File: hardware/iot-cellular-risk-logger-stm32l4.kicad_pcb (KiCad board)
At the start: 4 copper layers, 79 x 66.1 mm, 96 parts, among them J1 Nano SIM, J2 U.FL Antenna Connector (Male), J3 GSM_USB, J4 USB Type-C, J5 TagConnect SWD ARM, J6 GSM_DEBUG_UART, Q1 IRLML6401, Q2 DTC143Z, U1 STM32L433CBUx, U10 BGA 524N6 E6327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

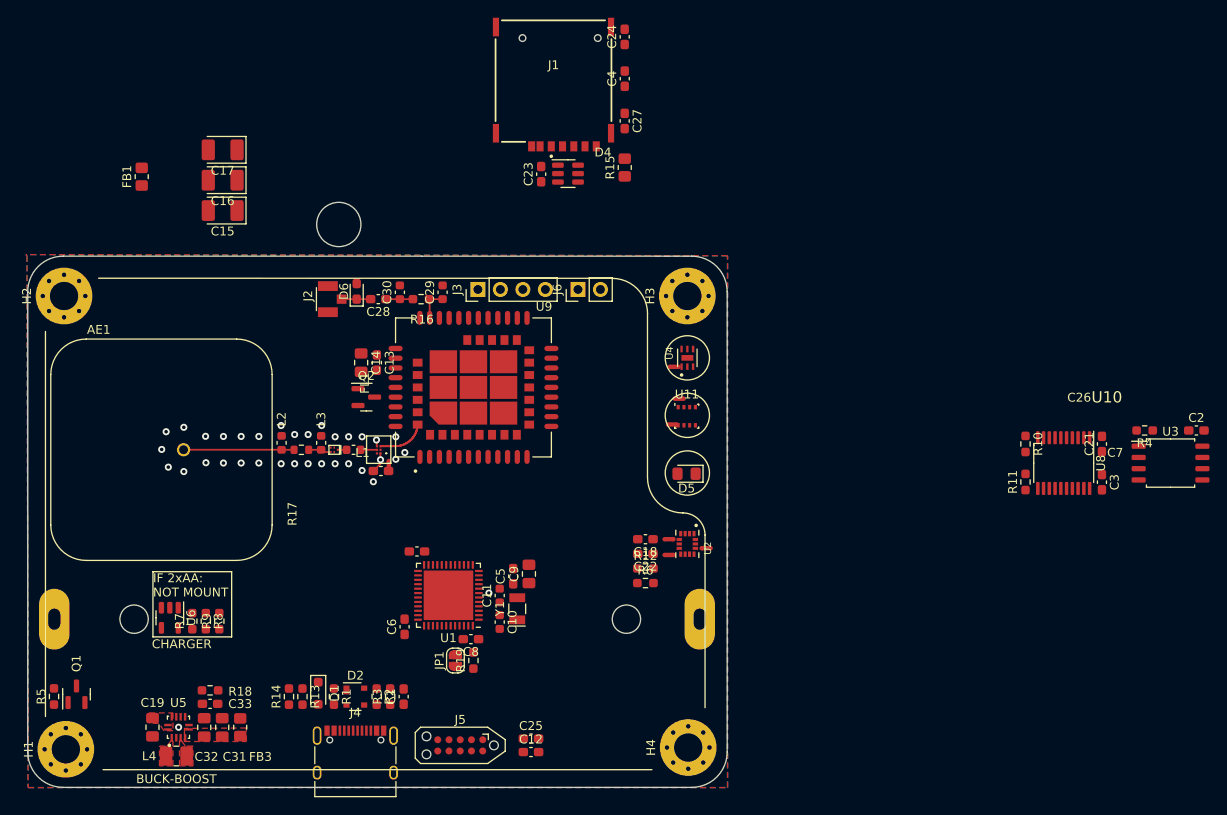
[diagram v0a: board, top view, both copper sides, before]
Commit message: Schema: split to hierarchical schema
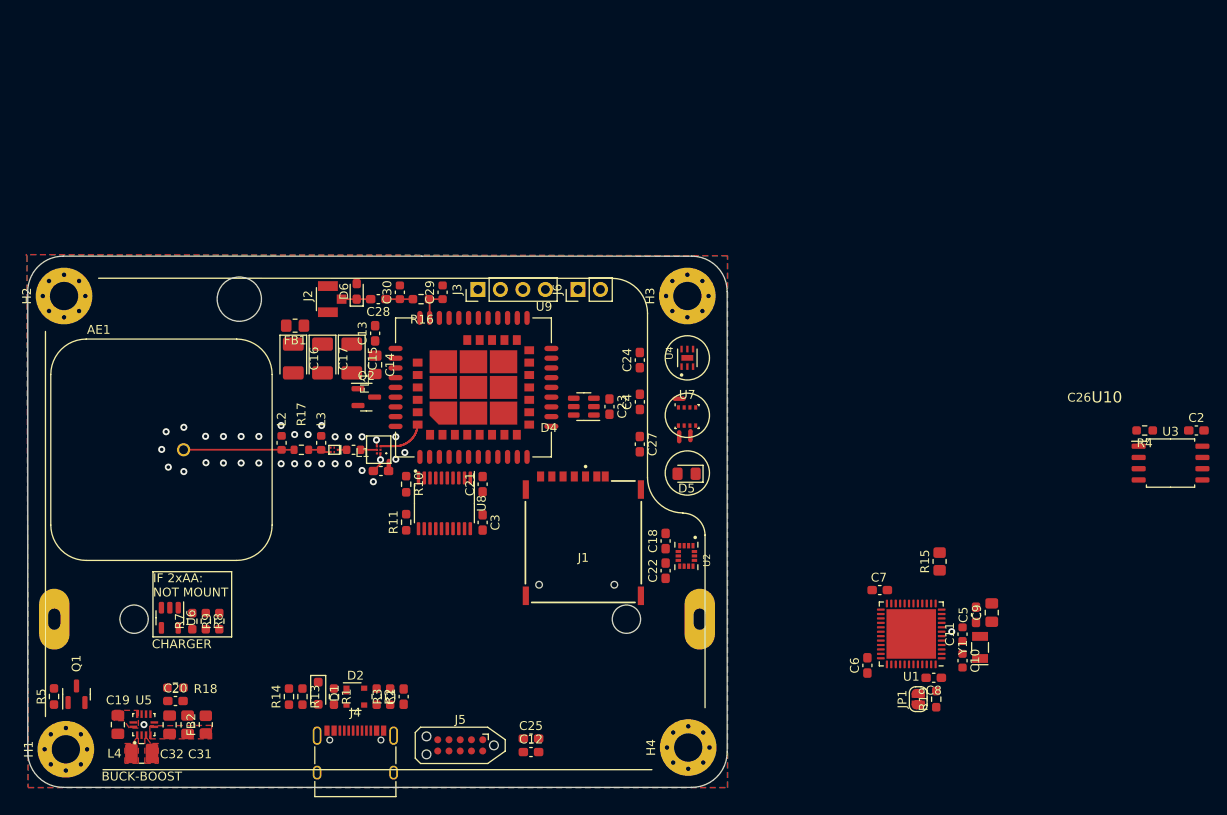
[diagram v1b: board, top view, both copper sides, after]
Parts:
- removed C33: 1n, Capacitor_SMD:C_0603_1608Metric_Pad1.08x0.95mm_HandSolder
- removed FB3: 330, Resistor_SMD:R_0805_2012Metric_Pad1.20x1.40mm_HandSolder
- removed NT4, NT5, NT7: NetTie_2, NetTie:NetTie-2_SMD_Pad0.5mm
- removed R12, R6: 4k7, Resistor_SMD:R_0603_1608Metric_Pad0.98x0.95mm_HandSolder
- removed U11: BME280, Package_LGA:Bosch_LGA-8_2.5x2.5mm_P0.65mm_ClockwisePinNumbering
- added C20: 1n, Capacitor_SMD:C_0603_1608Metric_Pad1.08x0.95mm_HandSolder, F.Cu at (59.2, 166.2)
- added FB2: 330, Resistor_SMD:R_0805_2012Metric_Pad1.20x1.40mm_HandSolder, F.Cu at (62.6, 168.9)
- added U7: BME280, Package_LGA:Bosch_LGA-8_2.5x2.5mm_P0.65mm_ClockwisePinNumbering, F.Cu at (117.0, 134.1)
- R5: value 100k -> 47k
- R8: value 47k -> 100k
- moved C21 70.1 mm to (93.9, 141.8)
- moved C3 70.1 mm to (93.9, 146.1)
- moved U8 70.1 mm to (89.6, 143.9)
- moved R10 70.1 mm to (85.2, 141.8)
- moved R11 70.1 mm to (85.2, 146.1)
- moved R15 57.0 mm to (145.5, 150.5)
- moved C7 52.5 mm to (138.7, 153.7)
- moved C8 52.5 mm to (144.8, 163.6)
- moved C10 52.5 mm to (148.1, 161.7)
- moved C11 52.5 mm to (148.1, 158.7)
- moved C5 52.5 mm to (149.6, 156.5)
- moved R19 52.5 mm to (145.1, 166.0)
- moved U1 52.5 mm to (142.3, 158.7)
- moved Y1 52.5 mm to (150.1, 160.2)
- moved C6 52.5 mm to (137.3, 162.2)
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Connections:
- net /+BATTERY renamed /Power Management Unit (PMU)/+BATTERY
- net /+GSM_VBAT renamed /GSM Module/+GSM_VBAT
- net /+LED renamed /MCU & Interfaces/+LED
- net /+VBUS renamed /MCU & Interfaces/+VBUS
- net /+VOUT renamed /Power Management Unit (PMU)/+VOUT
- net /BOOT0 renamed /MCU & Interfaces/BOOT0
- net /CLK renamed /GSM Module/CLK
- net /CTS renamed /GSM Module/CTS
- net /DATA renamed /GSM Module/DATA
- net /DCD renamed /GSM Module/DCD
- net /DTR renamed /GSM Module/DTR
- net /GND_SHIELD renamed /MCU & Interfaces/GND_SHIELD
- net /GNSS_ANT_RF renamed /GSM Module/GNSS_ANT_RF
- net /GNSS_M_RF renamed /GSM Module/GNSS_M_RF
- net /GSM_M_RF renamed /GSM Module/GSM_M_RF
- net /IND1 renamed /Power Management Unit (PMU)/IND1
- net /IND2 renamed /Power Management Unit (PMU)/IND2
- net /LNA_RF renamed /GSM Module/LNA_RF
- net /LSE IN renamed /MCU & Interfaces/LSE IN
- net /LSE OUT renamed /MCU & Interfaces/LSE OUT
- net /QSPI_CLK renamed /MCU & Interfaces/QSPI_CLK
- net /QSPI_IO0 renamed /MCU & Interfaces/QSPI_IO0
- net /QSPI_IO1 renamed /MCU & Interfaces/QSPI_IO1
- net /QSPI_IO2 renamed /MCU & Interfaces/QSPI_IO2
- net /QSPI_IO3 renamed /MCU & Interfaces/QSPI_IO3
- net /RI renamed /GSM Module/RI
- net /RST renamed /GSM Module/RST
- net /RTS renamed /GSM Module/RTS
- net /RX renamed /GSM Module/RX
- net /SAW_RF renamed /GSM Module/SAW_RF
- net /TX renamed /GSM Module/TX
- net /USB_CC1 renamed /MCU & Interfaces/USB_CC1
- net /USB_CC2 renamed /MCU & Interfaces/USB_CC2
- net /VCC_LNA renamed /GSM Module/VCC_LNA
- net /VDD renamed /GSM Module/VDD
- net /_QSPI_NCS renamed /MCU & Interfaces/_QSPI_NCS
- C28 pad 2: /GSM_ANT_RF -> /GSM Module/GSM_ANT_RF
- D5 pad 1: _LED -> /MCU & Interfaces/_LED
- D6 pad 1: /GSM_ANT_RF -> /GSM Module/GSM_ANT_RF
- H1 pad 1: unconnected-(H1-Pad1) -> GND
- H2 pad 1: unconnected-(H2-Pad1) -> GND
- H3 pad 1: unconnected-(H3-Pad1) -> GND
- H4 pad 1: unconnected-(H4-Pad1) -> GND
- NT1 pad 1: Net-(U2-VDD) -> Net-(U7-CSB)
- NT2 pad 1: Net-(U2-VDDIO) -> Net-(U7-VDD)
- NT3 pad 1: Net-(U11-CSB) -> Net-(U4-VDD)
- R5 pad 1: Net-(Q1-G) -> Net-(U6-STAT)
- R5 pad 2: GND -> CHARGE_STAT
- R8 pad 1: Net-(U6-STAT) -> Net-(Q1-G)
- R8 pad 2: CHARGE_STAT -> GND
- U1 pad 14: unconnected-(U1-PA4-Pad14) -> IMU_INT1
- U1 pad 15: unconnected-(U1-PA5-Pad15) -> IMU_INT2
- U1 pad 2: unconnected-(U1-PC13-Pad2) -> /MCU & Interfaces/_LED
- U1 pad 21: /RX3V -> /MCU & Interfaces/RX3V
- U1 pad 22: /TX3V -> /MCU & Interfaces/TX3V
- U1 pad 25: /RTS3V -> /MCU & Interfaces/RTS3V
- U1 pad 26: /CTS3V -> /MCU & Interfaces/CTS3V
- U1 pad 27: /RI3V -> /MCU & Interfaces/RI3V
- U1 pad 28: /DTR3V -> /MCU & Interfaces/DTR3V
- U1 pad 29: /DCD3V -> /MCU & Interfaces/DCD3V
- U1 pad 41: _LIGHT_INT -> unconnected-(U1-PB5-Pad41)
- U1 pad 42: IMU_INT1 -> _LIGHT_INT
- U1 pad 43: IMU_INT2 -> unconnected-(U1-PB7-Pad43)
- U2 pad 12: Net-(U2-CS) -> +3V3
- U2 pad 5: Net-(U2-VDDIO) -> +3V3
- U2 pad 8: Net-(U2-VDD) -> +3V3
- U8 pad 12: /RX3V -> /GSM Module/RX3V
- U8 pad 13: /TX3V -> /GSM Module/TX3V
- U8 pad 14: /RTS3V -> /GSM Module/RTS3V
- U8 pad 17: /CTS3V -> /GSM Module/CTS3V
- U8 pad 18: /DCD3V -> /GSM Module/DCD3V
- U8 pad 19: /DTR3V -> /GSM Module/DTR3V
- U8 pad 20: /RI3V -> /GSM Module/RI3V
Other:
- board size 79 x 66.1 mm -> 79 x 60 mm
